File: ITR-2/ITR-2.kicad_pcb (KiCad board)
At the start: 2 copper layers, 21 x 25 mm, 20 parts, among them X1 ico*группа_монтажных_отв.&1шт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, X2 ico*группа_монтажных_отв.&1шт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, X3 ico*группа_монтажных_отв.&1шт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, X4 ico*группа_монтажных_отв.&1шт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

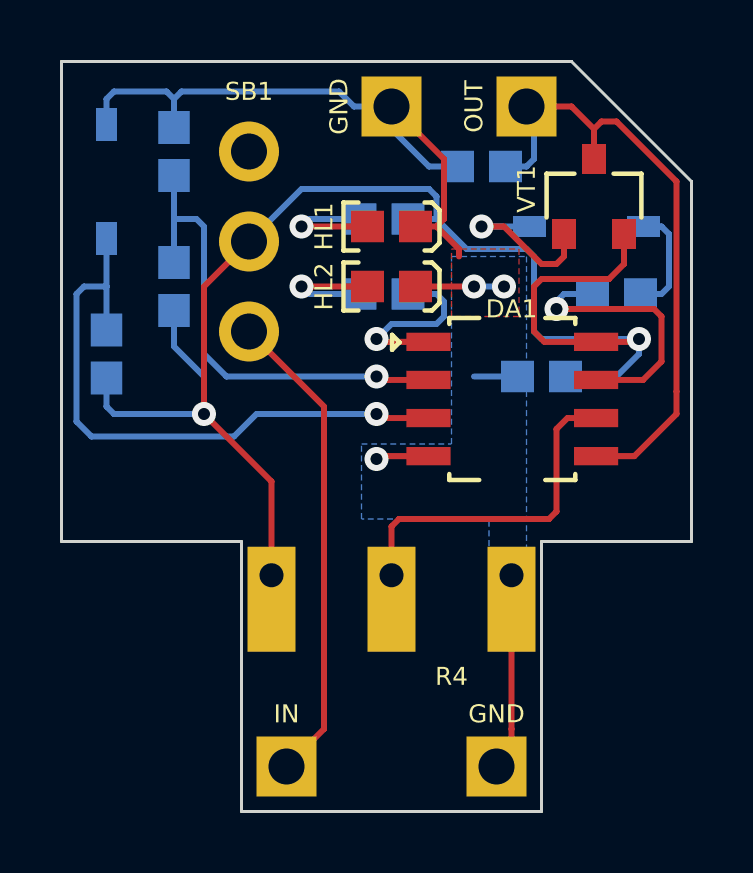
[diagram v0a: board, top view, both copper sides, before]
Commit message: исправления по результатам заказа: подтяжки на VT и Uout
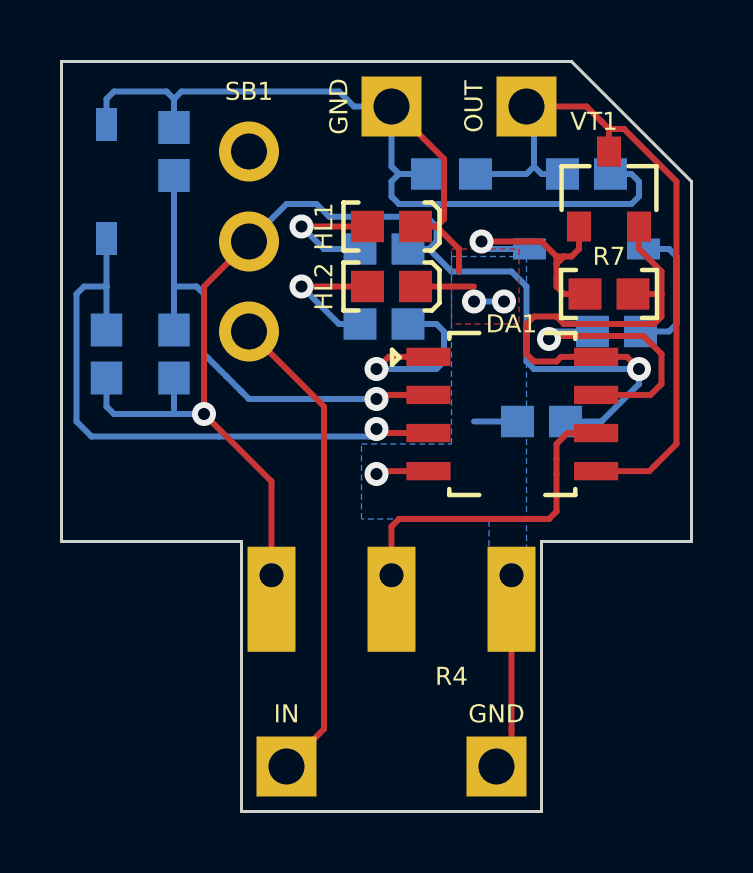
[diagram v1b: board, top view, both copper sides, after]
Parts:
- added R8: smd-резистор*4,7к*0603*ВП, KICAD6_RLC:Резистор_SMD_IEC_0603-0,1_Вт, B.Cu at (142.5, 92.0)
- added R9: smd-резистор*10к*0,1Вт*5проц*0603*ВП, KICAD6_RLC:Резистор_SMD_IEC_0603-0,1_Вт, B.Cu at (141.5, 86.8)
- R7: value smd-резистор*4,7к*0603*ВП -> smd-резистор*10к*0,1Вт*5проц*0603*ВП; moved to F.Cu
- moved R5 2.25 mm to (127.8, 92.8)
- moved C1 1.50 mm to (140.0, 95.0)
- moved C2 1.03 mm to (137.0, 86.8)
- moved R1 1.00 mm to (134.8, 89.2)
- moved R2 1.00 mm to (134.8, 91.8)
- moved VD2 0.75 mm to (141.5, 89.2)
- moved VT1 0.56 mm to (142.2, 87.2)
- moved DA1 0.50 mm to (136.3, 92.9)
- moved R7 0.25 mm to (142.2, 90.8), turned to 0 degrees
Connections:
- R7 pad 2: /DIRECT -> 9V
- VD2 pad A: Net-(R7-Pad1) -> Net-(R8-Pad1)
- VD2 pad K: Net-(VD2-PadK) -> Net-(R7-Pad1)
- VT1 pad 1: Net-(VD2-PadK) -> Net-(R7-Pad1)
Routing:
- net GND: track 34.6 -> 46.1 mm
- net Net-(VD2-PadK): track 5.72 -> 0.00 mm, vias 1 -> 0
- net Net-(R8-Pad1): track 0.00 -> 4.76 mm
- net Net-(R7-Pad1): track 3.76 -> 7.92 mm, vias 0 -> 1
- net /UOUT: track 21.2 -> 23.8 mm
- net 9V: track 52.1 -> 54.6 mm
- net /SENS: track 16.1 -> 17.8 mm
- net AREF: track 11.6 -> 11.1 mm
